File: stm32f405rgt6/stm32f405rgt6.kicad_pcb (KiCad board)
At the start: 4 copper layers, 87.6 x 73.7 mm, 41 parts, among them J1 USART, J2 SWD, J3 I2C, J4 USB_OTG, J5 SPI, J6 AnalogInptus, J7 5V, J7 5V and common GND, J8 CAN, J9 3.3V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

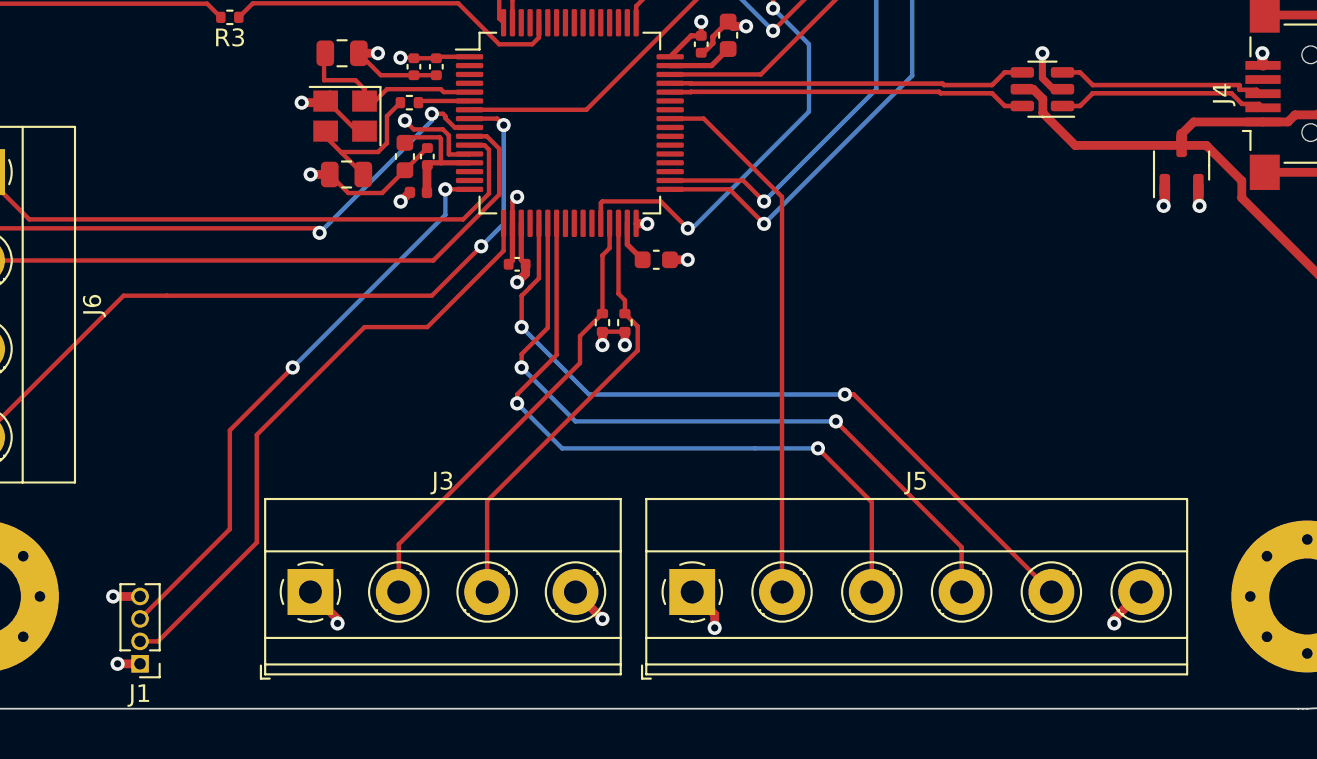
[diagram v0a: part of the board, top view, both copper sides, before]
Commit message: added caps to the voltage regulator also gerber and position files need to be updated
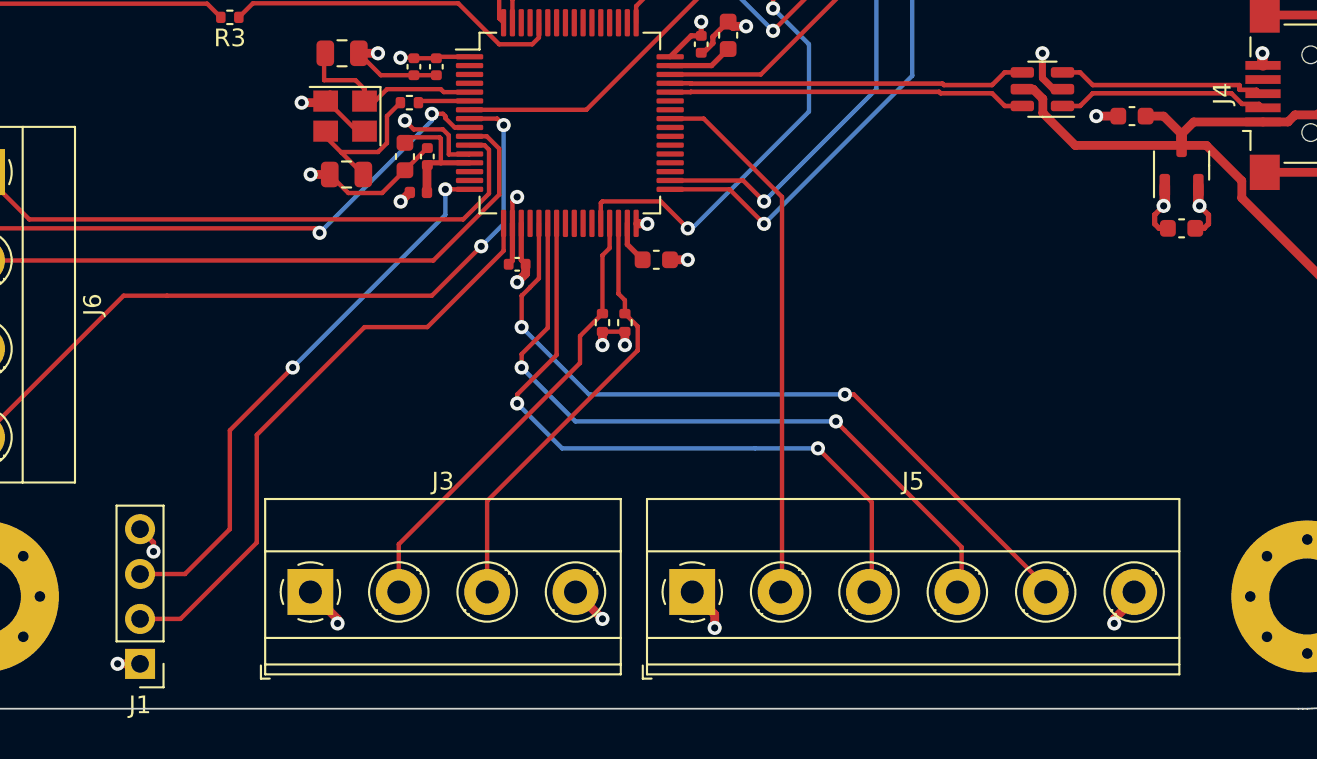
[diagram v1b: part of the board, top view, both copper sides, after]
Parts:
- added C14: 1u, Capacitor_SMD:C_0603_1608Metric, F.Cu at (195.3, 101.3)
- added C15: 1u, Capacitor_SMD:C_0603_1608Metric, F.Cu at (198.1, 107.7)
- J1: footprint Connector_PinHeader_1.27mm:PinHeader_1x04_P1.27mm_Vertical -> Connector_PinHeader_2.54mm:PinHeader_1x04_P2.54mm_Vertical
- J5: footprint TerminalBlock_Phoenix:TerminalBlock_Phoenix_MKDS-1,5-6-5.08_1x06_P5.08mm_Horizontal -> TerminalBlock_Phoenix:TerminalBlock_Phoenix_MKDS-1,5-6_1x06_P5.00mm_Horizontal
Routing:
- net GND: track 76.0 -> 79.4 mm, vias 26 -> 27
- net +5V: track 102.9 -> 105.3 mm
- net +3.3V: track 31.8 -> 33.9 mm
- net USART2_TX: track 32.8 -> 31.8 mm
- net USART2_RX: track 34.8 -> 34.3 mm
